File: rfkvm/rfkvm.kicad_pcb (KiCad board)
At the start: 2 copper layers, 134.6 x 53.3 mm, 18 parts, among them K1 G6SK-2, K2 G6SK-2, Q1 PN2222A, Q2 PN2222A, SW1 SW_Push, SW2 SW_Push, SW3 SW_Push, U1 USB-C Breakout, U2 USB-C Breakout, U3 USB-C Breakout

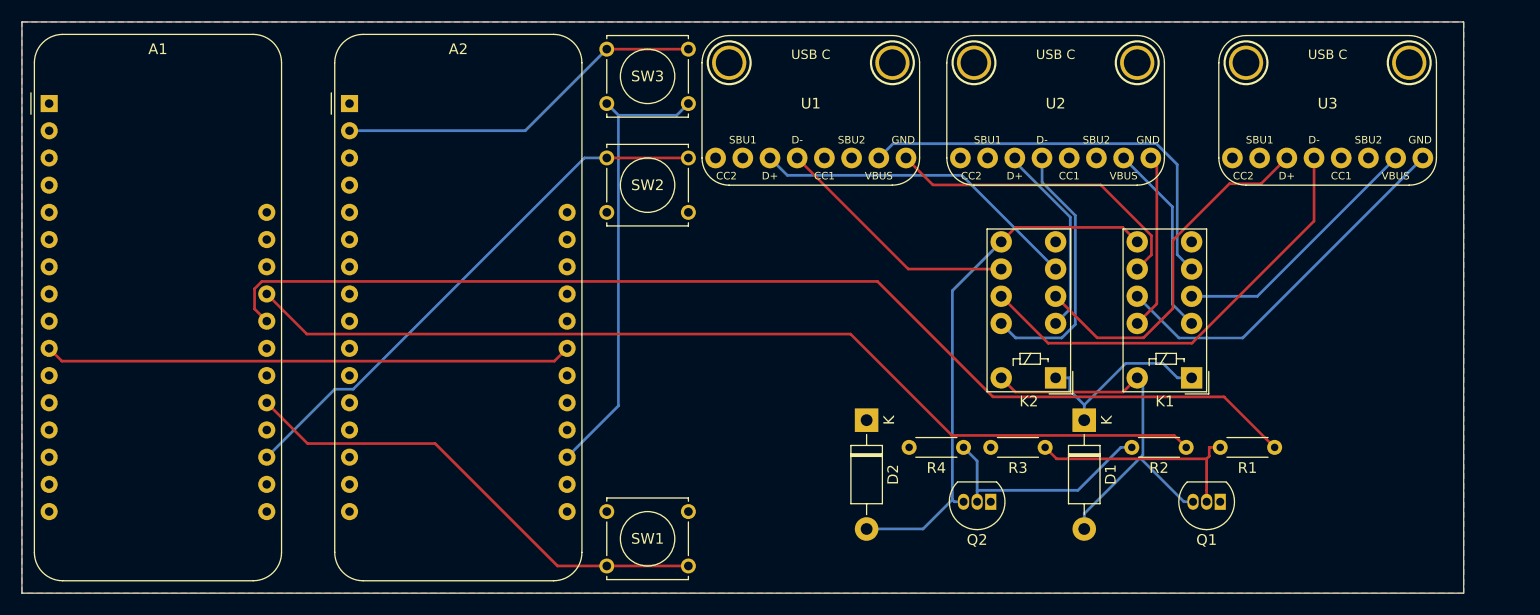
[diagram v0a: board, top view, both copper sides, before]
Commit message: Various updates and fixes * Only GND plane, no 3.3v plane, reduces complexity * Added text for version * Added graphics for fun * Fixed some alignments * Might have fixed some unconnected pads
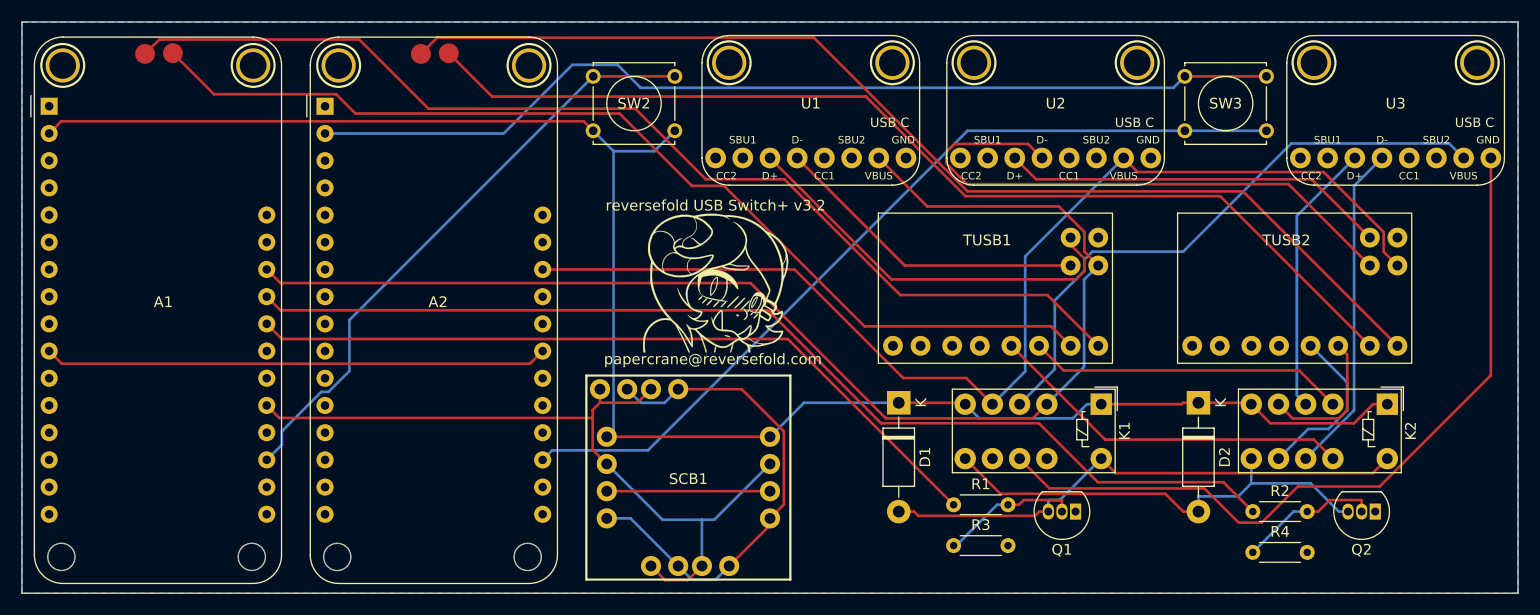
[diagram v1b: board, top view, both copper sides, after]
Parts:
- removed SW1: SW_Push, Button_Switch_THT:SW_Tactile_Straight_KSL0Axx1LFTR
- added SCB1: Sparkfun_Cherry_MX_Switch_Breakout, SparkFun:SparkFun Cherry MX Breakout, F.Cu at (151.1, 94.0)
- added TUSB1: tinkerBOY_USB_2.0_Hub, tinkerBOY:tinkerBOY USB 2.0 Hub, F.Cu at (168.9, 68.7)
- added TUSB2: tinkerBOY_USB_2.0_Hub, tinkerBOY:tinkerBOY USB 2.0 Hub, F.Cu at (196.8, 68.7)
- A1, A2: footprint Module:Adafruit_Feather -> Adafruit:Adafruit Feather RP2040
- moved SW3 54.0 mm to (197.5, 55.9)
- moved Q2 35.9 mm to (215.3, 96.5)
- moved K2 31.1 mm to (216.4, 86.5), turned to -90 degrees
- moved D2 31.0 mm to (198.8, 86.4)
- moved R1 30.5 mm to (175.9, 95.9), turned to 0 degrees
- moved R4 28.7 mm to (203.8, 100.3), turned to 0 degrees
- moved A1 22.2 mm to (102.9, 77.5)
- moved A2 21.1 mm to (128.6, 77.5)
- moved D1 17.4 mm to (170.8, 86.4)
- moved Q1 13.5 mm to (187.3, 96.5)
- moved R3 12.5 mm to (175.9, 99.7), turned to 0 degrees
- moved K1 8.79 mm to (189.7, 86.5), turned to -90 degrees
- moved R2 8.64 mm to (203.8, 96.5), turned to 0 degrees
- moved SW2 7.73 mm to (142.2, 55.9)
- moved U3 6.35 mm to (217.2, 58.4)
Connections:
- A1 pad 26: unconnected-(A1-Pad26) -> Net-(A1-Pad26)
- A2 pad 26: unconnected-(A2-Pad26) -> Net-(A2-Pad26)
- D1 pad 1: Net-(D1-Pad1) -> +3V3
- K1 pad 1: Net-(D1-Pad1) -> +3V3
- K1 pad 10: Net-(K1-Pad10) -> GND
- K1 pad 3: Net-(K1-Pad3) -> Net-(A1-Pad26)
- K1 pad 5: Net-(K1-Pad5) -> Net-(A2-Pad26)
- K1 pad 8: Net-(K1-Pad8) -> GND
- K2 pad 1: Net-(D1-Pad1) -> +3V3
- U1 pad 1: Net-(K1-Pad8) -> GND
- U1 pad 2: Net-(K1-Pad5) -> Net-(A1-Pad26)
- U1 pad 5: Net-(K2-Pad8) -> Net-(TUSB1-Pad1)
- U1 pad 6: Net-(K2-Pad5) -> Net-(TUSB1-Pad0)
- U2 pad 1: Net-(K1-Pad10) -> GND
- U2 pad 2: Net-(K1-Pad3) -> Net-(A2-Pad26)
- U2 pad 5: Net-(K2-Pad10) -> Net-(TUSB2-Pad1)
- U2 pad 6: Net-(K2-Pad3) -> Net-(TUSB2-Pad0)
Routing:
- net +3V3: track 0.00 -> 164.7 mm
- net Net-(A1-Pad26): track 0.00 -> 119.8 mm
- net Net-(A2-Pad26): track 0.00 -> 106.1 mm
- net Net-(A2-Pad29): track 0.00 -> 103.7 mm
- net Net-(A1-Pad29): track 0.00 -> 101.4 mm
- net Net-(A2-Pad30): track 0.00 -> 97.3 mm
- net Net-(A1-Pad30): track 0.00 -> 95.1 mm
- net Net-(A2-Pad2): track 34.8 -> 91.9 mm
- net Net-(TUSB2-Pad1): track 0.00 -> 54.3 mm
- net unconnected-(SCB1-Pad4): track 0.00 -> 46.3 mm
- net Net-(K1-Pad5): track 39.5 -> 0.00 mm
- net Net-(TUSB1-Pad0): track 0.00 -> 38.0 mm
- net Net-(A2-Pad19): track 42.4 -> 80.3 mm
- net Net-(K1-Pad9): track 35.2 -> 72.5 mm
- net Net-(TUSB2-Pad0): track 0.00 -> 36.2 mm
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- removed copper zone on F.Cu, net +3V3
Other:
- board size 134.6 x 53.3 mm -> 139.7 x 53.3 mm
- board text added: "papercrane@reversefold.com"
- board text added: "reversefold USB Switch+ v3.2"
